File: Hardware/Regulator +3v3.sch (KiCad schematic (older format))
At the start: 7 parts, among them U1 AOZ1280CI

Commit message: Add 5v regulator and RS485 transceiver to Main board
Added RS485 and a 5v regulator to power it
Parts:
- added C5: 10nF, symbol Capacitor
- added C6: 10uF, symbol Capacitor
- added D?: DIODESCH, ~, symbol DIODESCH
- added L?: 2.2uH, ~, symbol INDUCTOR
- added R3: 49.9k, symbol Resistor
- added R4: 9.53k, symbol Resistor
- added U?: AOZ1280CI, symbol AOZ1280CI
- C2, C3: symbol CAPACITOR -> Capacitor
- R1: symbol RESISTOR -> Resistor
- R2: value 15.8 -> 15.8k; symbol RESISTOR -> Resistor
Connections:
- net labels added: REG2EN, Reg+5V
- wire segments 19 -> 52

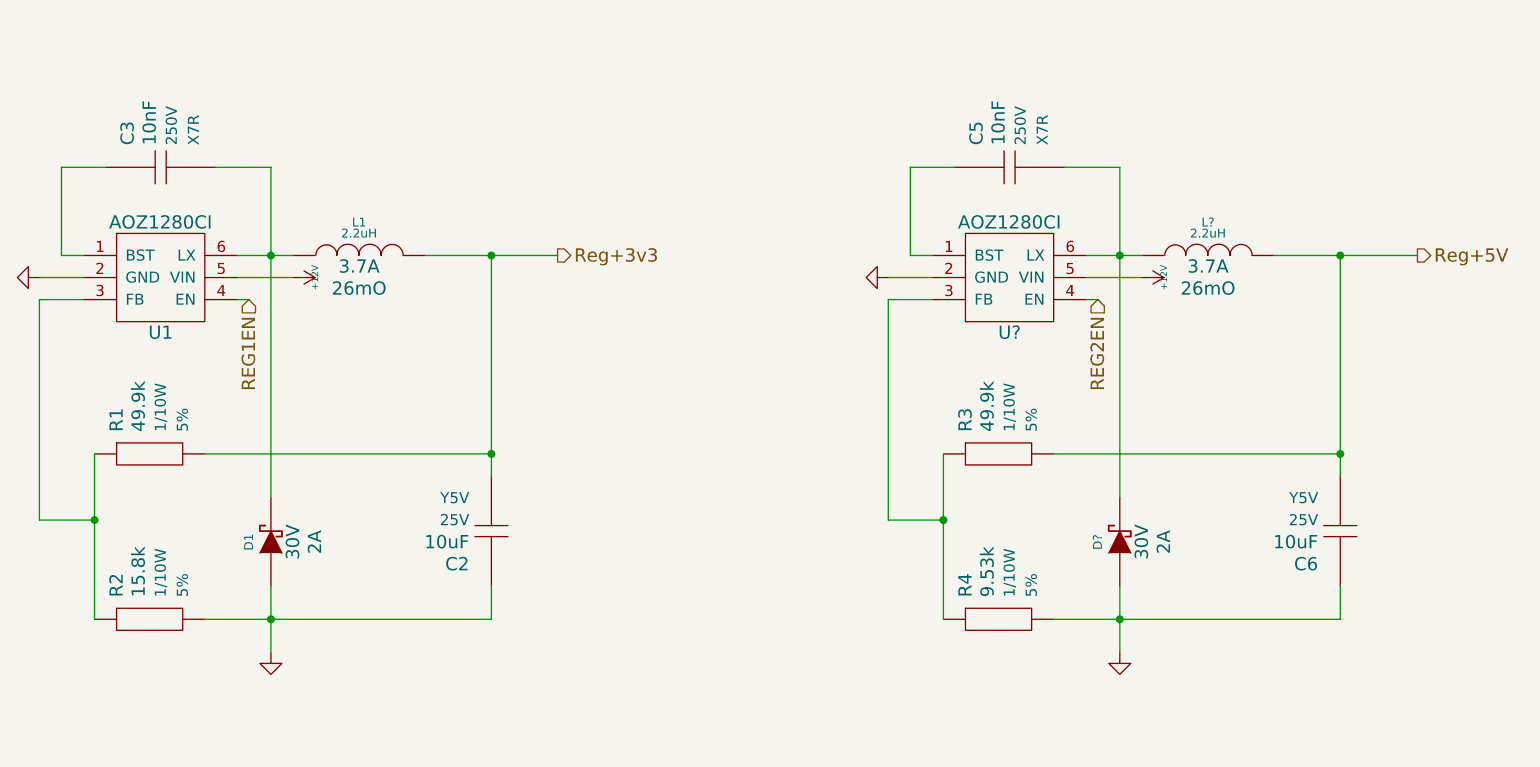
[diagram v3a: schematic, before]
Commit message: Add GPS Pads, potentiometer to INA125, 3v3 regulator always enabled, footprints created for GPS Pads and BTA, parts assigned
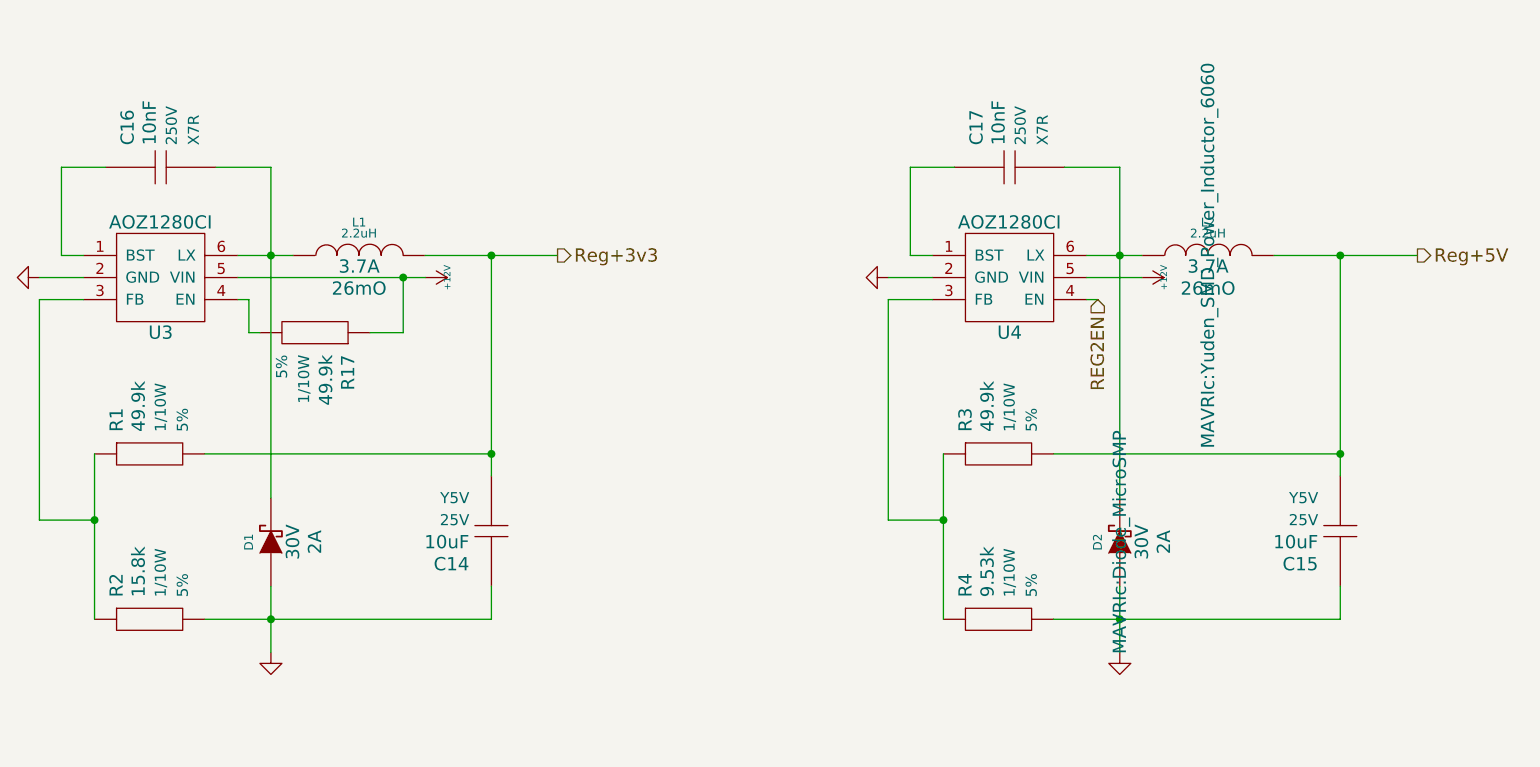
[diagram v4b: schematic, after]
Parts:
- added R17: 49.9k, Resistors_SMD:R_1206_HandSoldering, symbol Resistor
- C14: renamed from C2; footprint (none) -> Capacitors_SMD:C_1206_HandSoldering
- C15: renamed from C6; footprint (none) -> Capacitors_SMD:C_1206_HandSoldering
- C16: renamed from C3; footprint (none) -> Capacitors_SMD:C_1206_HandSoldering
- C17: renamed from C5; footprint (none) -> Capacitors_SMD:C_1206_HandSoldering
- D1: footprint ~ -> MAVRIc:Diode_MicroSMP
- D2: renamed from D?; footprint ~ -> MAVRIc:Diode_MicroSMP
- L1: footprint ~ -> MAVRIc:Yuden_SMD_Power_Inductor_6060
- L2: renamed from L?; footprint ~ -> MAVRIc:Yuden_SMD_Power_Inductor_6060
- R1, R2, R3, R4: footprint (none) -> Resistors_SMD:R_1206_HandSoldering
- U3: renamed from U1; footprint (none) -> Housings_SOT-23_SOT-143_TSOT-6:SOT-23-6
- U4: renamed from U?; footprint (none) -> Housings_SOT-23_SOT-143_TSOT-6:SOT-23-6
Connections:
- net +12V: now also R17.1
- net REG1EN: no longer names the net of U3.4 (EN)
- net REG1EN: now also R17.2
